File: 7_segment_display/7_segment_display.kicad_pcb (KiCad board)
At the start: 2 copper layers, 33 x 20.3 mm, 15 parts, among them J1 Conn_01x05_Male, J2 Conn_01x05_Female, U1 74HC595, U2 SBC18-11SURKCGKWA

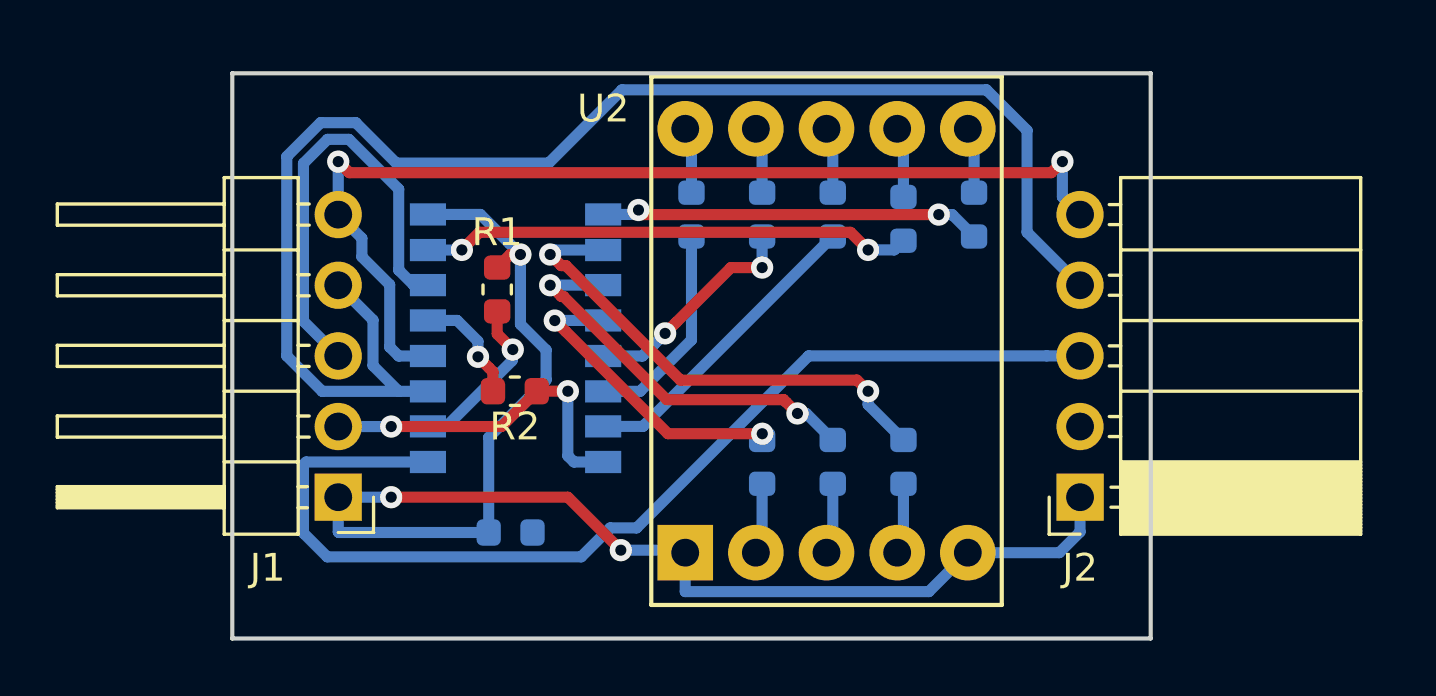
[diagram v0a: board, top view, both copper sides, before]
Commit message: Make one that actually works
Use correct pin footprint for 7 segment display
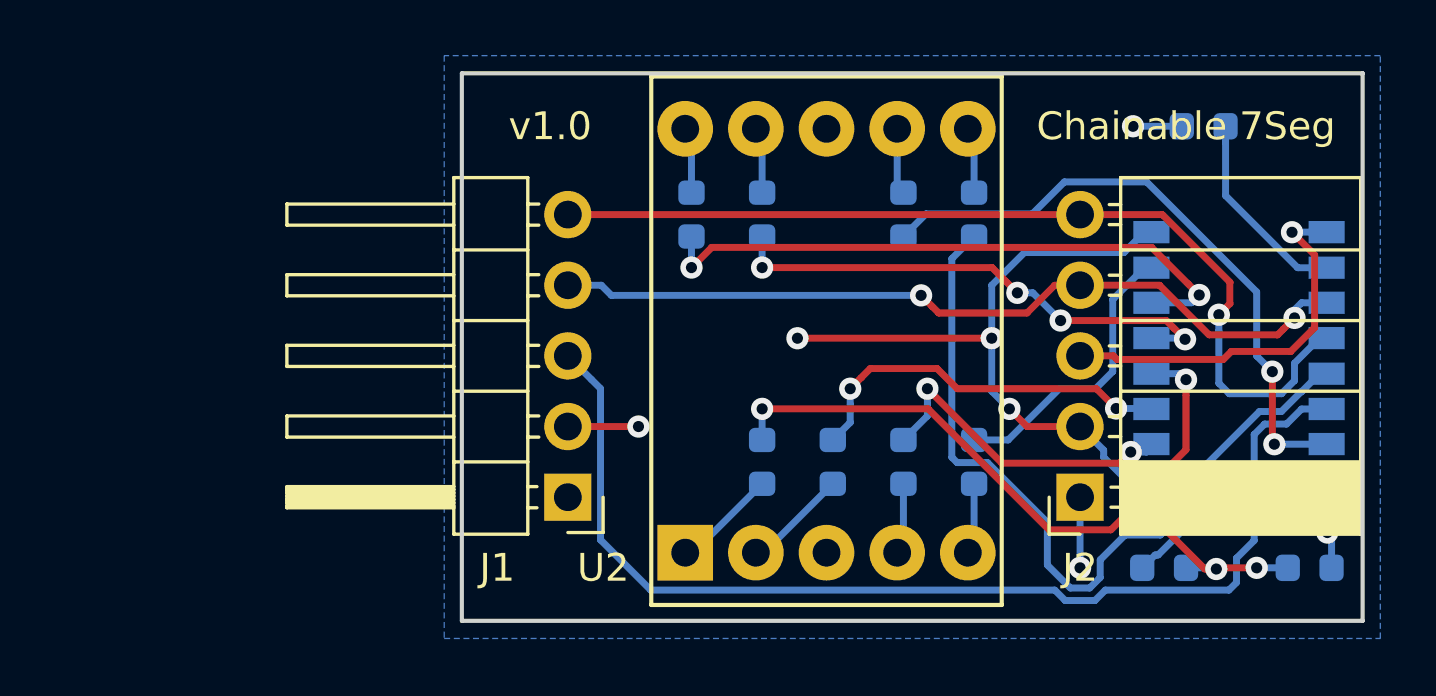
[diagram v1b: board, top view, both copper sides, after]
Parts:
- R1, R2: moved to B.Cu
- U2: value SBC18-11SURKCGKWA -> 5611BH_7_Segment_Display_Common_Cathode
- moved C1 28.8 mm to (38.7, 17.8), turned to 180 degrees
- moved R1 26.1 mm to (34.9, 1.91), turned to 0 degrees
- moved U1 26.0 mm to (36.2, 10.2), turned to 0 degrees
- moved R2 24.2 mm to (33.5, 17.8)
- moved R10 10.2 mm to (26.7, 14.0), turned to 90 degrees
- moved J1 8.25 mm to (12.1, 15.2)
- moved R3 0.15 mm to (24.1, 5.08)
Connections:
- U2 pad 1: +3V3 -> Net-(R7-Pad1)
- U2 pad 2: Net-(R7-Pad1) -> Net-(R6-Pad1)
- U2 pad 3: Net-(R6-Pad1) -> +3V3
- U2 pad 5: +3V3 -> Net-(R10-Pad1)
- U2 pad 8: Net-(R10-Pad1) -> +3V3
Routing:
- net +3V3: track 53.9 -> 7.54 mm
- net /SER_OUT: track 38.2 -> 14.0 mm, vias 0 -> 1
- net /SRCLK: track 53.3 -> 29.5 mm, vias 0 -> 2
- net /SER_IN: track 16.1 -> 39.7 mm
- net GND: track 12.5 -> 34.9 mm, vias 2 -> 7
- net /7SEG_G: track 7.66 -> 22.2 mm, vias 0 -> 2
- net /7SEG_E: track 11.1 -> 23.3 mm
- net /7SEG_F: track 8.15 -> 18.6 mm, vias 2 -> 4
- net /7SEG_B: track 13.8 -> 22.2 mm, vias 2 -> 0
- net Net-(R2-Pad1): track 4.13 -> 10.4 mm, vias 1 -> 0
- net /7SEG_C: track 17.7 -> 11.7 mm
- net /7SEG_A: track 17.8 -> 22.8 mm
- net /RCLK: track 37.5 -> 33.8 mm, vias 2 -> 1
- net Net-(R7-Pad1): track 2.57 -> 3.79 mm
- net Net-(R6-Pad1): track 2.57 -> 3.79 mm
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- added copper zone on F.Cu, net +3V3
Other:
- board size 33 x 20.3 mm -> 32.4 x 19.7 mm
- board text added: "Chainable 7Seg"
- board text added: "v1.0"
